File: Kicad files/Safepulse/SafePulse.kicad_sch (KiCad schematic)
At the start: 87 parts, among them IC1 S-35770E01I-K8T2U, J1 Conn_01x03_Male, J2 4208, Q1 FQT7N10L, Q2 BC846A, Q3 MMBT3906, Q4 MMBT3906, U1 TS4061AILT-1.25, U2 74HC14, U3 TLV27L1DBVT, U33 MAX9910EXK+T, U4 CD14538BM

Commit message: Updated with LCSC numbers
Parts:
- C1: LCSC (none) -> C520084
- C10, C11, C12, C13, C14, C15, C16, C17, C18, C6, C7, C8, C9: LCSC (none) -> C710458
- C19, C2, C23, C27, C4, C5: LCSC (none) -> C1713
- C22: LCSC (none) -> C1717; LCSC Part # C1818 -> C1717
- C24: LCSC (none) -> C97905
- C25: LCSC (none) -> C19110; LCSC Part # C97905 -> C19110
- C3: LCSC (none) -> C83170; LCSC Part # C277515 -> C83170
- D1, D2: LCSC (none) -> C282360
- D3, D4, D5, D6, D7, D8, D9: LCSC (none) -> C151049
- F1: LCSC (none) -> C20978
- FB1, FB2: LCSC (none) -> C515370
- L1: LCSC (none) -> C5289366; LCSC Part # C2043159 -> C5289366
- Q1: LCSC (none) -> C154506
- Q2: LCSC (none) -> C507907
- Q3, Q4: LCSC (none) -> C53444
- R1: LCSC (none) -> C488845
- R10, R7, R8, R9: LCSC (none) -> C34719
- R11: LCSC (none) -> C242487; LCSC Part # C242487 -> C17633
- R12, R25, R5: LCSC (none) -> C328380
- R13, R19, R3: LCSC (none) -> C96346
- R14: LCSC (none) -> C865422; LCSC Part # C325883 -> C865422
- R15: LCSC (none) -> C104108
- R16: LCSC (none) -> C107700
- R17: LCSC (none) -> C317482
- R18: LCSC (none) -> C95781
- R20: LCSC (none) -> C228266; LCSC Part # C228266 -> C2999465
- R21: LCSC (none) -> C328397
- R22: LCSC (none) -> C17444; LCSC Part # C163977 -> C17444
- R23, R27: LCSC (none) -> C332788
- R24: LCSC (none) -> C352242
- R4: LCSC (none) -> C161788; LCSC Part # C161788 -> C17414
- R6: LCSC (none) -> C17438; LCSC Part # C844393 -> C17438
- U1: LCSC (none) -> C2157484
- U2: LCSC (none) -> C232776
- U33: LCSC (none) -> C2057992
- U4: LCSC (none) -> C2652506

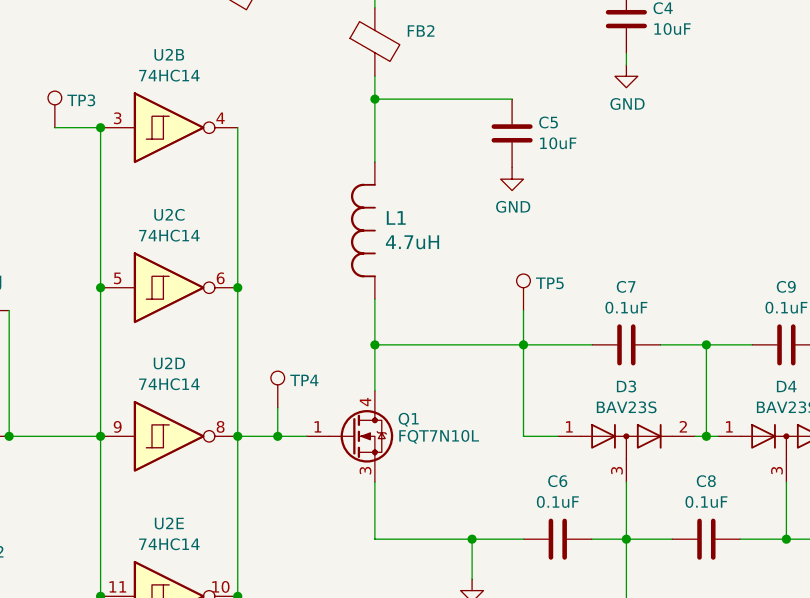
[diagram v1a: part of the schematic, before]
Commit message: Updated for JLC part numbers and stock
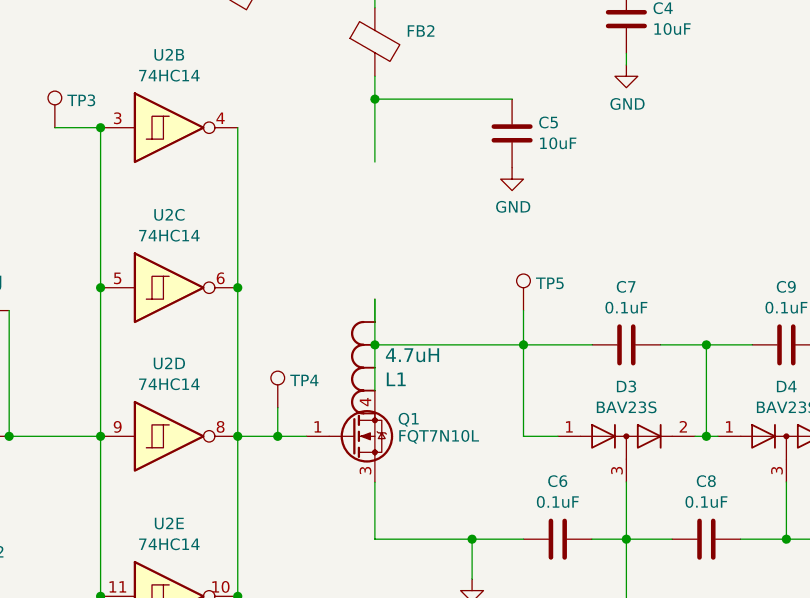
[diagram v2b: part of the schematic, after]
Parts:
- U3: LCSC (none) -> C2868527
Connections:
- net at C5.1, FB2.2: no longer L1.1
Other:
- moved on the sheet: L1
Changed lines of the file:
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@@
 		(lib_id "2021-01-06_02-33-04:NRS6020T2R2NMGJ")
 		(at 115.57 57.785 90)
+		(mirror x)
 		(unit 1)
 		(exclude_from_sim no)
@@
 		(dnp no)
 		(property "Reference" "L1"
-			(at 116.6876 48.8188 90)
+			(at 116.6876 66.7512 90)
 			(effects
 				(font
@@
 		)
 		(property "Value" "4.7uH"
-			(at 116.688 51.511 90)
+			(at 116.688 64.059 90)
 			(effects
 				(font
@@
 		)
 		(property "Footprint" "Inductor_SMD:L_Taiyo-Yuden_MD-4040"
-			(at 122.809 50.8 0)
+			(at 122.809 64.77 0)
 			(effects
 				(font
@@
 		)
 		(property "LCSC" "C5289366"
-			(at 116.6876 48.8188 0)
+			(at 116.6876 66.7512 0)
 			(effects
 				(font
@@
 			(effects
 				(font
+					(size 1.27 1.27)
+				)
+				(hide yes)
+			)
+		)
+		(property "LCSC" "C2868527"
+			(at 52.07 160.6549 0)
+			(effects
+				(font
